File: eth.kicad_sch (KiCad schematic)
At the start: 34 parts, among them J6 RJ45_Abracon_ARJP11A-MASA-B-A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, U26 LAN8742A, U27 USBLC6-4SC6, Y2 25MHz

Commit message: v 0.2 schematics
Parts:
- removed L?: 22u, symbol Device:L
- added C?: 100n, Capacitor_SMD:C_0603_1608Metric, symbol Device:C
- added C? (x2): 10u, Capacitor_SMD:C_0805_2012Metric, symbol Device:C
- added C?: 220u, Capacitor_Tantalum_SMD:CP_EIA-7343-15_Kemet-W, symbol Device:C_Polarized
- added FB11: 1K@100MHz, Inductor_SMD:L_1210_3225Metric, symbol Device:FerriteBead_Small
- added L?: 1u, Inductor_SMD:L_1008_2520Metric, symbol Device:L
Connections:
- net +3V3: now also L?.2
- net AVDDT_PHY: now also FB11.1
- net GND: now also C?.2, C?.2, C?.2, C?.2
- net PHY_TD_N: now also U27.6 (I/O4); no longer U27.4 (I/O3)
- net PHY_TD_P: now also U27.4 (I/O3); no longer U27.6 (I/O4)
- net POE_VC+: now also J6.10 (V-); no longer J6.9 (V+)
- net POE_VC-: now also J6.9 (V+); no longer J6.10 (V-)
- new net: C?.1, C?.1, C?.1, C?.1, FB11.2, L?.1
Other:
- moved on the sheet: C162, C163, C164, C165, C166, C167, C168, C169, C170, C171, J6, R73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

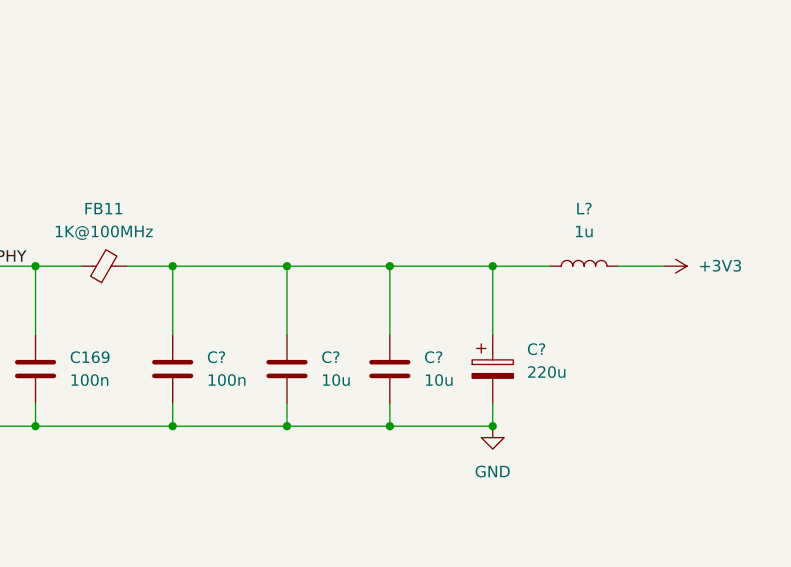
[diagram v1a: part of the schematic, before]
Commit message: change damper
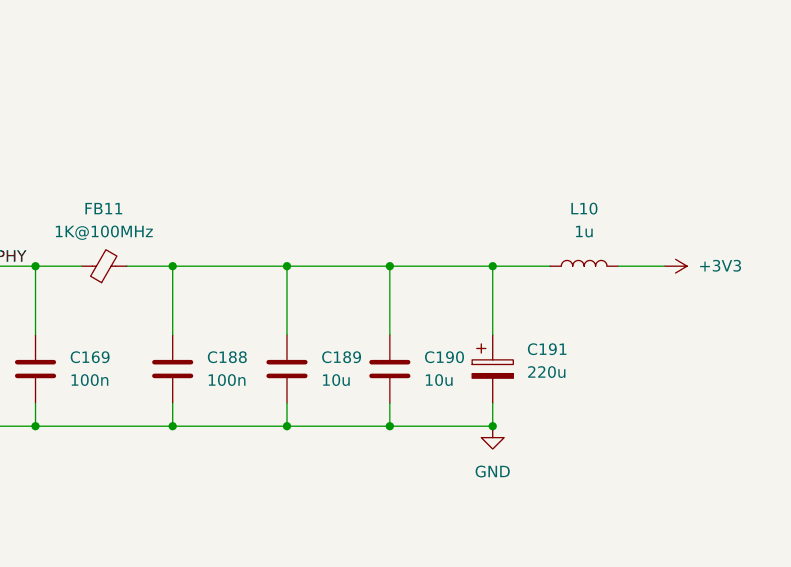
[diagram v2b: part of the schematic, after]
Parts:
- gave numbers to parts that had none: 5
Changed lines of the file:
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@@
   (symbol (lib_id "Device:L") (at 322.58 184.15 90) (unit 1)
     (in_bom yes) (on_board yes) (fields_autoplaced)
-    (property "Reference" "L?" (id 0) (at 322.58 177.8 90))
+    (property "Reference" "L10" (id 0) (at 322.58 177.8 90))
     (property "Value" "1u" (id 1) (at 322.58 180.34 90))
     (property "Footprint" "Inductor_SMD:L_1008_2520Metric" (id 2) (at 322.58 184.15 0)
@@
   (symbol (lib_id "Device:C") (at 276.86 195.58 0) (unit 1)
     (in_bom yes) (on_board yes) (fields_autoplaced)
-    (property "Reference" "C?" (id 0) (at 280.67 194.3099 0)
+    (property "Reference" "C188" (id 0) (at 280.67 194.3099 0)
       (effects (font (size 1.27 1.27)) (justify left))
     )
@@
   (symbol (lib_id "Device:C") (at 300.99 195.58 0) (unit 1)
     (in_bom yes) (on_board yes) (fields_autoplaced)
-    (property "Reference" "C?" (id 0) (at 304.8 194.3099 0)
+    (property "Reference" "C190" (id 0) (at 304.8 194.3099 0)
       (effects (font (size 1.27 1.27)) (justify left))
     )
@@
   (symbol (lib_id "Device:C_Polarized") (at 312.42 195.58 0) (unit 1)
     (in_bom yes) (on_board yes) (fields_autoplaced)
-    (property "Reference" "C?" (id 0) (at 316.23 193.4209 0)
+    (property "Reference" "C191" (id 0) (at 316.23 193.4209 0)
       (effects (font (size 1.27 1.27)) (justify left))
     )
@@
   (symbol (lib_id "Device:C") (at 289.56 195.58 0) (unit 1)
     (in_bom yes) (on_board yes) (fields_autoplaced)
-    (property "Reference" "C?" (id 0) (at 293.37 194.3099 0)
-      (effects (font (size 1.27 1.27)) (justify left))
-    )
+    (property "Reference" "C189" (id 0) (at 293.37 194.3099 0)
+      (effects (font (size 1.27 1.27)) (justify left))
+    )

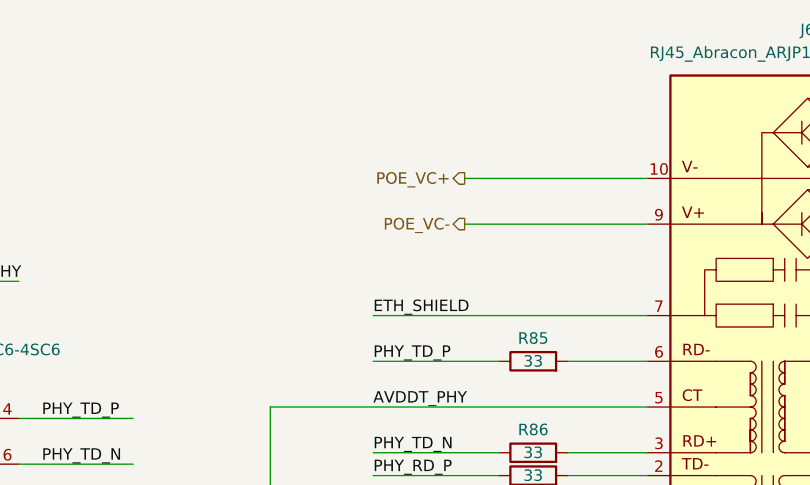
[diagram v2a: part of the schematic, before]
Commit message: import sch to pcb
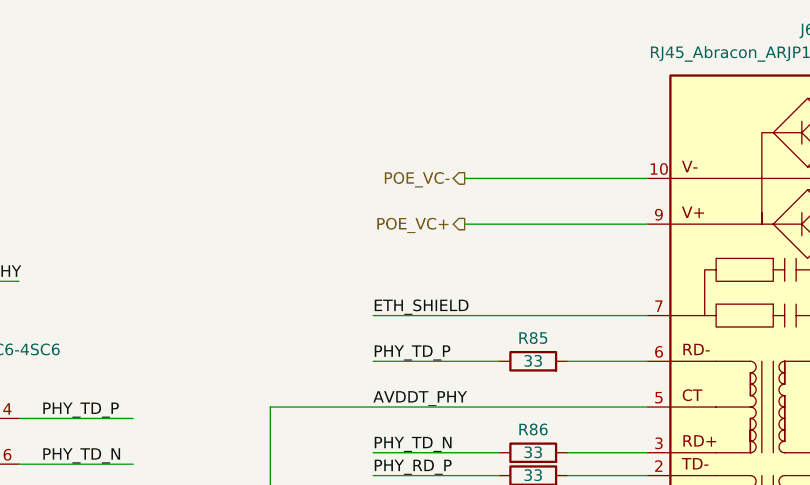
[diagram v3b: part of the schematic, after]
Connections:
- net POE_VC+: now also J6.9 (V+); no longer J6.10 (V-)
- net POE_VC-: now also J6.10 (V-); no longer J6.9 (V+)
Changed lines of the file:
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@@
     (effects (font (size 1.27 1.27)) (justify right))
   )
-  (hierarchical_label "POE_VC-" (shape output) (at 264.16 69.85 180)
+  (hierarchical_label "POE_VC-" (shape output) (at 264.16 64.77 180)
     (effects (font (size 1.27 1.27)) (justify right))
   )
@@
     (effects (font (size 1.27 1.27)) (justify right))
   )
-  (hierarchical_label "POE_VC+" (shape output) (at 264.16 64.77 180)
+  (hierarchical_label "POE_VC+" (shape output) (at 264.16 69.85 180)
     (effects (font (size 1.27 1.27)) (justify right))
   )

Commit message: fix eth
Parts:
- added R107, R108, R109, R110: 100, Resistor_SMD:R_0603_1608Metric, symbol Device:R
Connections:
- net GND: now also R107.1, R108.1, R109.2, R110.2
- net PHY_RD_N: now also R85.1, R108.2; no longer R88.1
- net PHY_RD_P: now also R86.1, R107.2; no longer R87.1
- net PHY_TD_N: now also R87.1, R110.1; no longer R86.1
- net PHY_TD_P: now also R88.1, R109.1; no longer R85.1
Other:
- moved on the sheet: U27

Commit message: placement v2
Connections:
- net PHY_TD_N: now also R109.1, U27.4 (I/O3); no longer R110.1, U27.6 (I/O4)
- net PHY_TD_P: now also R110.1, U27.6 (I/O4); no longer R109.1, U27.4 (I/O3)
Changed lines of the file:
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@@
     (effects (font (size 1.27 1.27)) (justify left bottom))
   )
-  (label "PHY_TD_N" (at 170.18 96.52 0)
+  (label "PHY_TD_N" (at 170.18 91.44 0)
     (effects (font (size 1.27 1.27)) (justify left bottom))
   )
@@
     (effects (font (size 1.27 1.27)) (justify left bottom))
   )
-  (label "PHY_TD_P" (at 170.18 91.44 0)
+  (label "PHY_TD_P" (at 170.18 96.52 0)
     (effects (font (size 1.27 1.27)) (justify left bottom))
   )
